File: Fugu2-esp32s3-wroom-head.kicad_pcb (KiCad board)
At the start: 2 copper layers, 26 x 23.7 mm, 19 parts, among them J1 Conn_02x03_ESP_PROG, J2 Conn_02x07_Odd_Even, P1 USB4105-GF-A, SW1 SW_Push, U1 ESP32-S3-WROOM-1, U2 TLV70233_SOT23-5

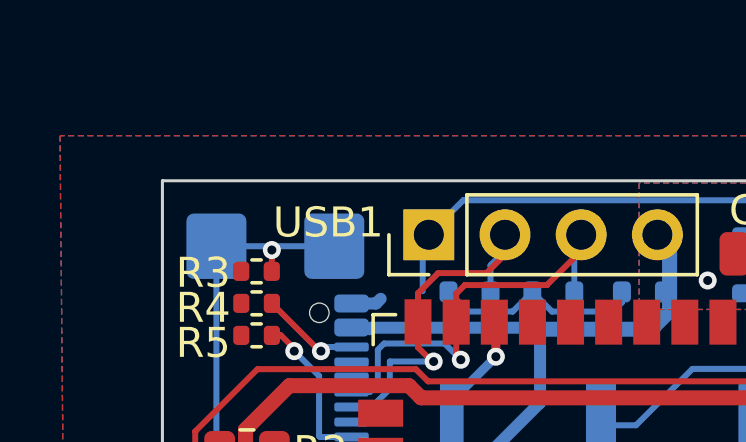
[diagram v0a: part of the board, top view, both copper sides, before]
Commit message: add 3d renderings
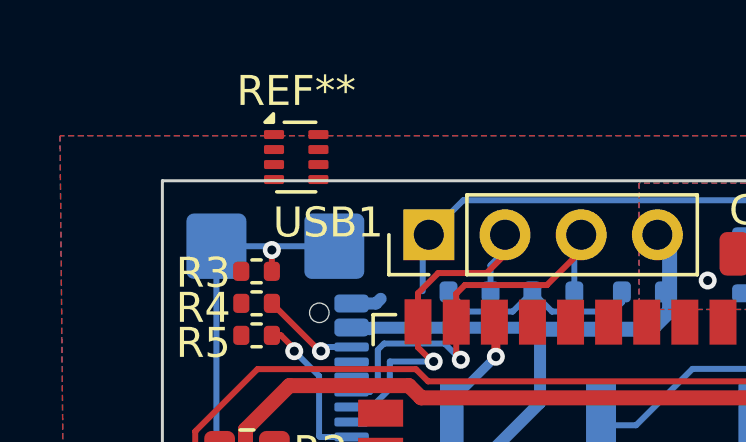
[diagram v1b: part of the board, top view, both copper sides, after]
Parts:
- added REF**: SOT-583-8, Package_TO_SOT_SMD:SOT-583-8, F.Cu at (98.3, 36.8)
